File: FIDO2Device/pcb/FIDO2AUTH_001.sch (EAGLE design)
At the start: 31 parts, among them CN1 TE-1734028, CN2 IF_5PIN_H, SW1 SKRPACE010, SW2 SKTADAE010, U1 MDBT50Q-P1M, U2 XC6206P332MR-G, X1 NX3215SA-32.768K

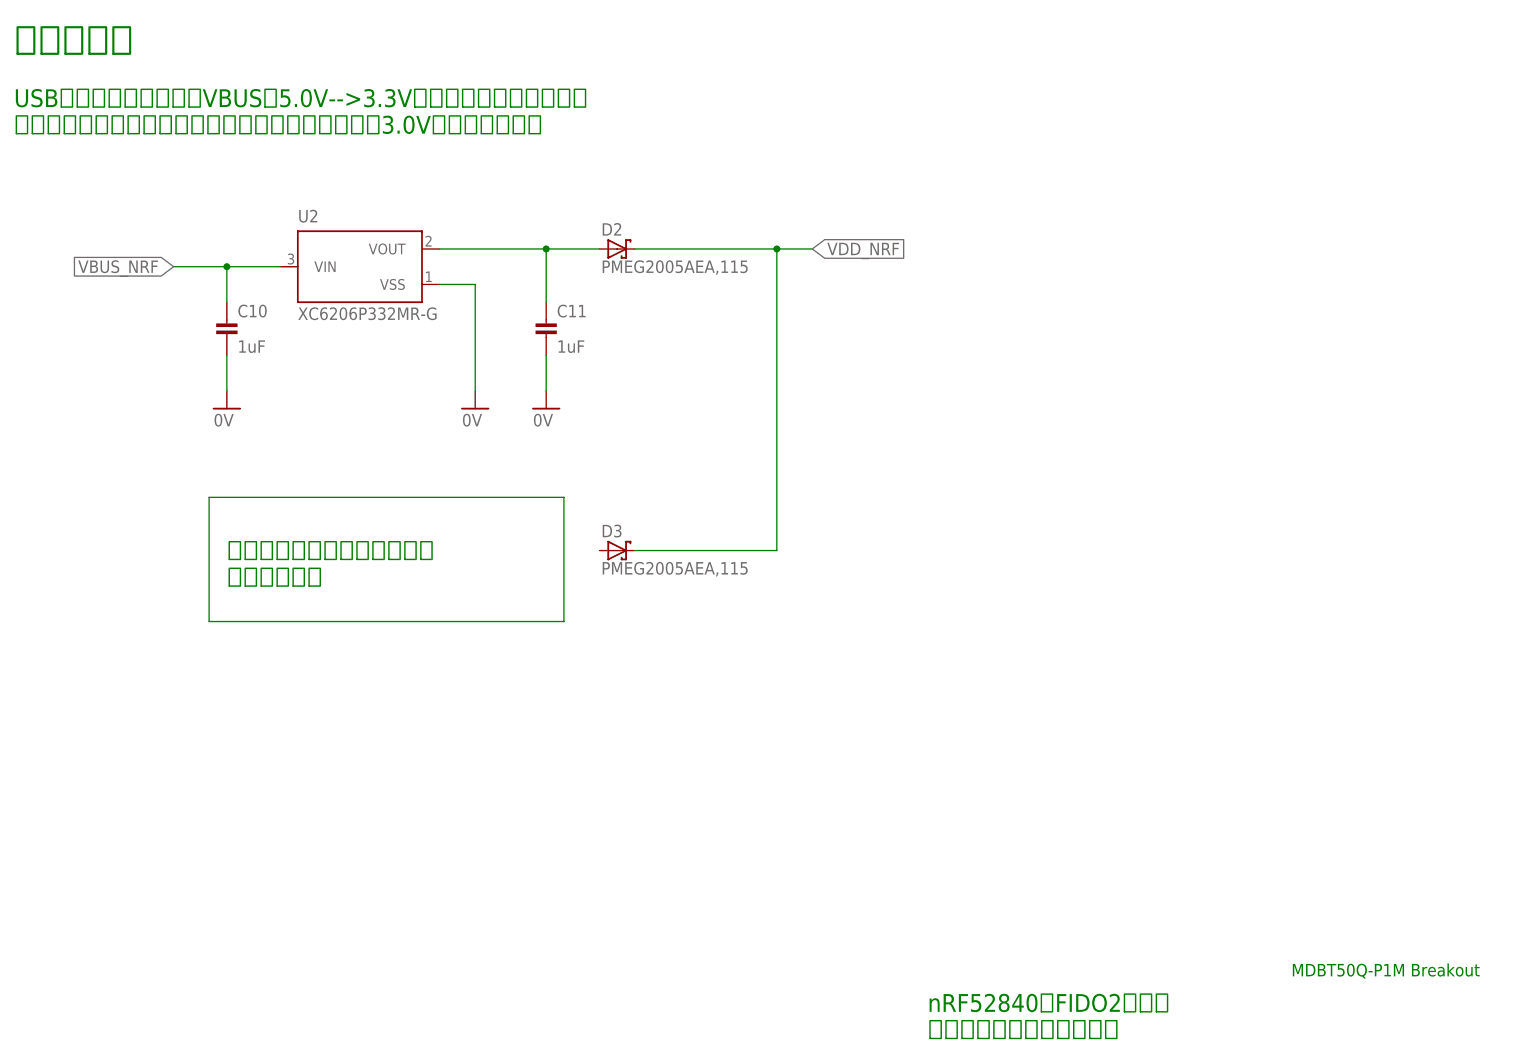
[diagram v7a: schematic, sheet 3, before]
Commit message: [WIP] ブレークアウト基板回路図
・電池ホルダー（CR1225用、3.0V）を追加
・汎用I/O用のヘッダーピン（3Pin）を追加
・プリント基板上の配線作業を開始
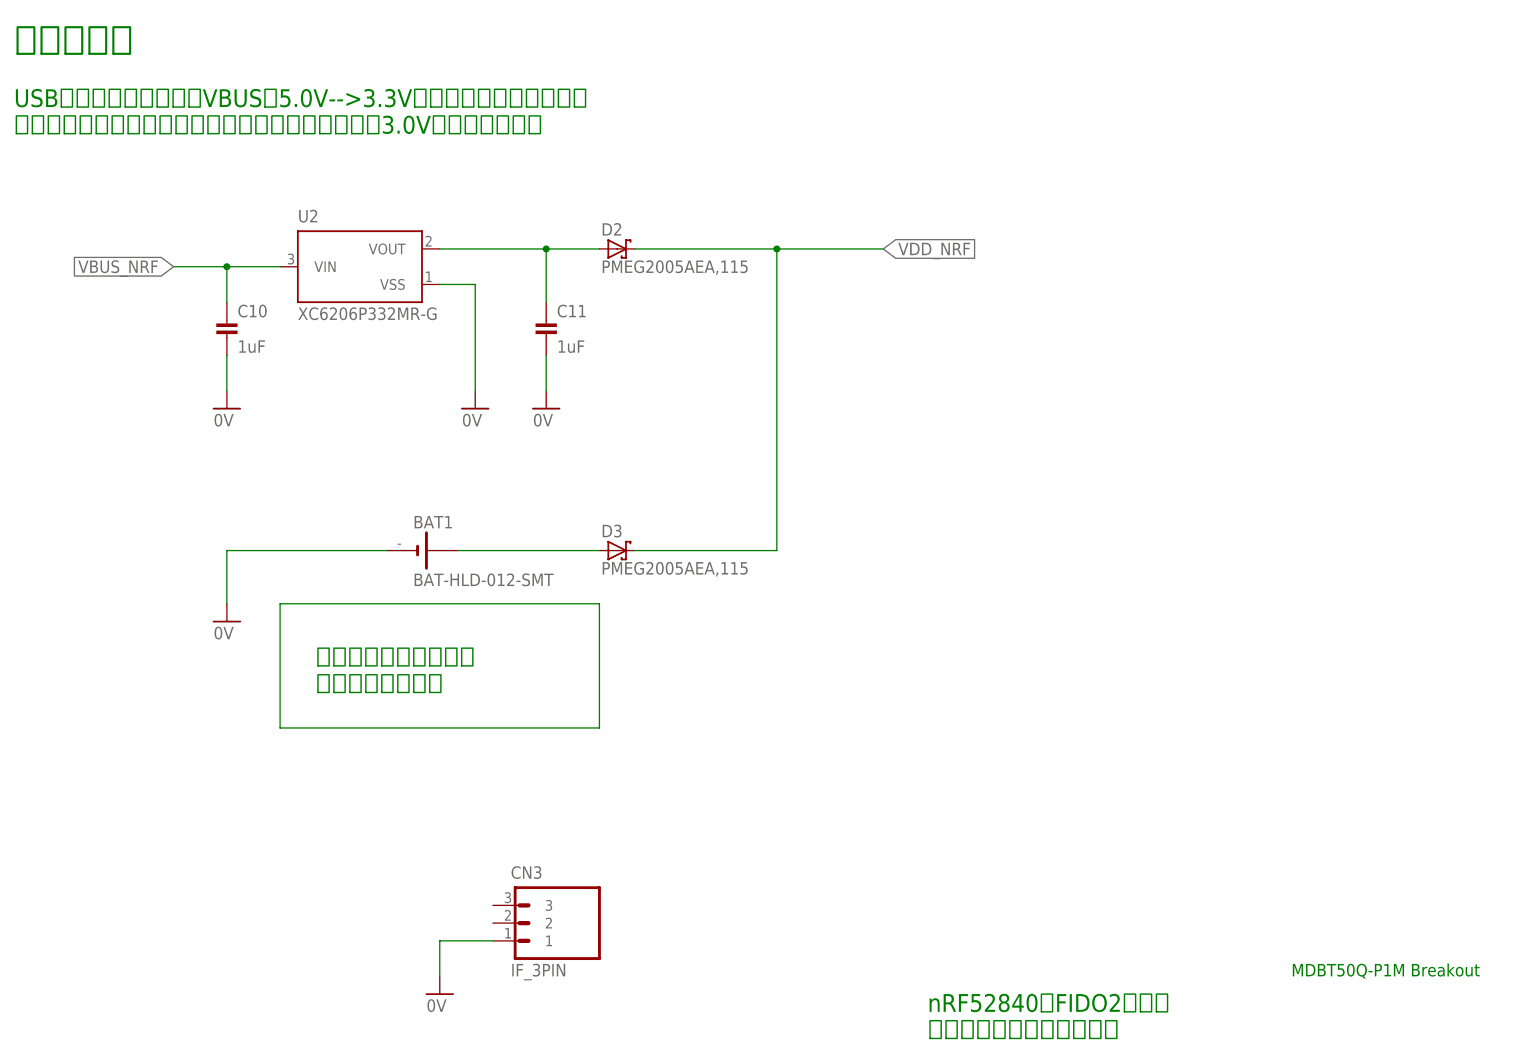
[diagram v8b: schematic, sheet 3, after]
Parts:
- added BAT1: BAT-HLD-012-SMT, Connectors:BAT-HLD-012-SMT
- added CN3: IF_3PIN, Connectors:IF_3PIN
- C7, C8, C9: device Parts:CAP_0402 -> Parts:CAP_0603
- R1, R2, R3, R4, R5: device Parts:RESISTOR_0402 -> Parts:RESISTOR_0603
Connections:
- new net N$5: BAT1.+, D3.A
- net 0V: now also BAT1.-, CN3.1
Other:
- note added: "ボタン乾電池ケースは 基板の背面に実装"
- note removed: "ここにボタン乾電池ケースを 追加します。"
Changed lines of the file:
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@@
 <part name="C5" library="Parts" deviceset="CAP" device="_0603" value="0.01uF"/>
 <part name="C6" library="Parts" deviceset="CAP" device="_0603" value="10uF"/>
-<part name="C7" library="Parts" deviceset="CAP" device="_0402" value="0.1uF"/>
-<part name="C8" library="Parts" deviceset="CAP" device="_0402" value="0.1uF"/>
+<part name="C7" library="Parts" deviceset="CAP" device="_0603" value="0.1uF"/>
+<part name="C8" library="Parts" deviceset="CAP" device="_0603" value="0.1uF"/>
 <part name="GND8" library="Supply" deviceset="0V" device=""/>
 <part name="GND9" library="Supply" deviceset="0V" device=""/>
@@
 <part name="D1" library="Parts" deviceset="PRTR5V0U2X" device=""/>
 <part name="CN1" library="Connectors" deviceset="TE-1734028" device=""/>
-<part name="R1" library="Parts" deviceset="RESISTOR" device="_0402" value="10k"/>
-<part name="C9" library="Parts" deviceset="CAP" device="_0402" value="0.1uF"/>
+<part name="R1" library="Parts" deviceset="RESISTOR" device="_0603" value="10k"/>
+<part name="C9" library="Parts" deviceset="CAP" device="_0603" value="0.1uF"/>
 <part name="GND11" library="Supply" deviceset="0V" device=""/>
 <part name="SW1" library="Parts" deviceset="SKRPACE010" device=""/>
@@
 <part name="LED1" library="Parts" deviceset="APHD1608" device="LSURCK"/>
 <part name="LED2" library="Parts" deviceset="APHF1608" device="LSEEQBDZGKC"/>
-<part name="R2" library="Parts" deviceset="RESISTOR" device="_0402" value="1.5k"/>
-<part name="R3" library="Parts" deviceset="RESISTOR" device="_0402" value="1.2k"/>
-<part name="R4" library="Parts" deviceset="RESISTOR" device="_0402" value="2.2k"/>
-<part name="R5" library="Parts" deviceset="RESISTOR" device="_0402" value="390"/>
+<part name="R2" library="Parts" deviceset="RESISTOR" device="_0603" value="1.5k"/>
+<part name="R3" library="Parts" deviceset="RESISTOR" device="_0603" value="1.2k"/>
+<part name="R4" library="Parts" deviceset="RESISTOR" device="_0603" value="2.2k"/>
+<part name="R5" library="Parts" deviceset="RESISTOR" device="_0603" value="390"/>
 <part name="CN2" library="Connectors" deviceset="IF_5PIN" device="_H"/>
 <part name="GND14" library="Supply" deviceset="0V" device=""/>
@@
 <part name="D2" library="Parts" deviceset="PMEG2005" device="AEA,115"/>
 <part name="D3" library="Parts" deviceset="PMEG2005" device="AEA,115"/>
+<part name="BAT1" library="Connectors" deviceset="BAT-HLD-012-SMT" device=""/>
+<part name="GND18" library="Supply" deviceset="0V" device=""/>
+<part name="CN3" library="Connectors" deviceset="IF_3PIN" device=""/>
+<part name="GND19" library="Supply" deviceset="0V" device=""/>
 </parts>
 <sheets>
@@
 <text x="35.56" y="147.32" size="2.54" layer="91" align="top-left">USBポートに装着時は、VBUSの5.0V--&gt;3.3Vに降圧して供給します。
 乾電池ホルダーにボタン乾電池を装着した場合は、3.0Vを供給します。</text>
-<text x="66.04" y="76.2" size="2.54" layer="91">ここにボタン乾電池ケースを
-追加します。</text>
+<text x="78.74" y="60.96" size="2.54" layer="91">ボタン乾電池ケースは
+基板の背面に実装</text>
 </plain>
 <instances>
@@
 <instance part="D2" gate="G$1" x="121.92" y="124.46"/>
 <instance part="D3" gate="G$1" x="121.92" y="81.28"/>
+<instance part="BAT1" gate="G$1" x="93.98" y="81.28"/>
+<instance part="GND18" gate="1" x="66.04" y="71.12"/>
+<instance part="CN3" gate="G$1" x="104.14" y="30.48"/>
+<instance part="GND19" gate="1" x="96.52" y="17.78"/>
 </instances>
 <busses>
@@
 <pinref part="GND17" gate="1" pin="0V"/>
 <wire x1="111.76" y1="109.22" x2="111.76" y2="104.14" width="0.1524" layer="91"/>
+</segment>
+<segment>
+<pinref part="BAT1" gate="G$1" pin="-"/>
+<pinref part="GND18" gate="1" pin="0V"/>
+<wire x1="88.9" y1="81.28" x2="66.04" y2="81.28" width="0.1524" layer="91"/>
+<wire x1="66.04" y1="81.28" x2="66.04" y2="73.66" width="0.1524" layer="91"/>
+</segment>
+<segment>
+<pinref part="CN3" gate="G$1" pin="1"/>
+<pinref part="GND19" gate="1" pin="0V"/>
+<wire x1="104.14" y1="25.4" x2="96.52" y2="25.4" width="0.1524" layer="91"/>
+<wire x1="96.52" y1="25.4" x2="96.52" y2="20.32" width="0.1524" layer="91"/>
 </segment>
 </net>
@@
 <segment>
 <wire x1="124.46" y1="124.46" x2="144.78" y2="124.46" width="0.1524" layer="91"/>
-<label x="149.86" y="124.46" size="1.778" layer="95" xref="yes"/>
+<label x="160.02" y="124.46" size="1.778" layer="95" xref="yes"/>
 <pinref part="D2" gate="G$1" pin="C"/>
 <pinref part="D3" gate="G$1" pin="C"/>
-<wire x1="144.78" y1="124.46" x2="149.86" y2="124.46" width="0.1524" layer="91"/>
+<wire x1="144.78" y1="124.46" x2="160.02" y2="124.46" width="0.1524" layer="91"/>
 <wire x1="124.46" y1="81.28" x2="144.78" y2="81.28" width="0.1524" layer="91"/>
 <wire x1="144.78" y1="81.28" x2="144.78" y2="124.46" width="0.1524" layer="91"/>
@@
 <net name="N$1" class="0">
 <segment>
-<wire x1="63.5" y1="88.9" x2="114.3" y2="88.9" width="0.1524" layer="91"/>
-<wire x1="114.3" y1="88.9" x2="114.3" y2="71.12" width="0.1524" layer="91"/>
-<wire x1="114.3" y1="71.12" x2="63.5" y2="71.12" width="0.1524" layer="91"/>
-<wire x1="63.5" y1="71.12" x2="63.5" y2="88.9" width="0.1524" layer="91"/>
-</segment>
-</net>
+<wire x1="73.66" y1="73.66" x2="119.38" y2="73.66" width="0.1524" layer="91"/>
+<wire x1="119.38" y1="73.66" x2="119.38" y2="55.88" width="0.1524" layer="91"/>
+<wire x1="119.38" y1="55.88" x2="73.66" y2="55.88" width="0.1524" layer="91"/>
+<wire x1="73.66" y1="55.88" x2="73.66" y2="73.66" width="0.1524" layer="91"/>
+</segment>
+</net>
+<net name="N$5" class="0">
+<segment>
+<pinref part="BAT1" gate="G$1" pin="+"/>
+<pinref part="D3" gate="G$1" pin="A"/>
+<wire x1="99.06" y1="81.28" x2="119.38" y2="81.28" width="0.1524" layer="91"/>
+</segment>
+</net>
